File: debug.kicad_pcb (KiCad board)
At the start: 2 copper layers, 56.4 x 42.2 mm, 47 parts, among them J1 ZX62D-AB-5P8, P1 LPC-Link, P2 UART, P3 JTAG, P4 Cortex-Debug, P5 Vout, U1 93C46, U2 PRTR5V0U2X, U3 FT2232H, U4 LD1117S33CTR, X1 12MHz

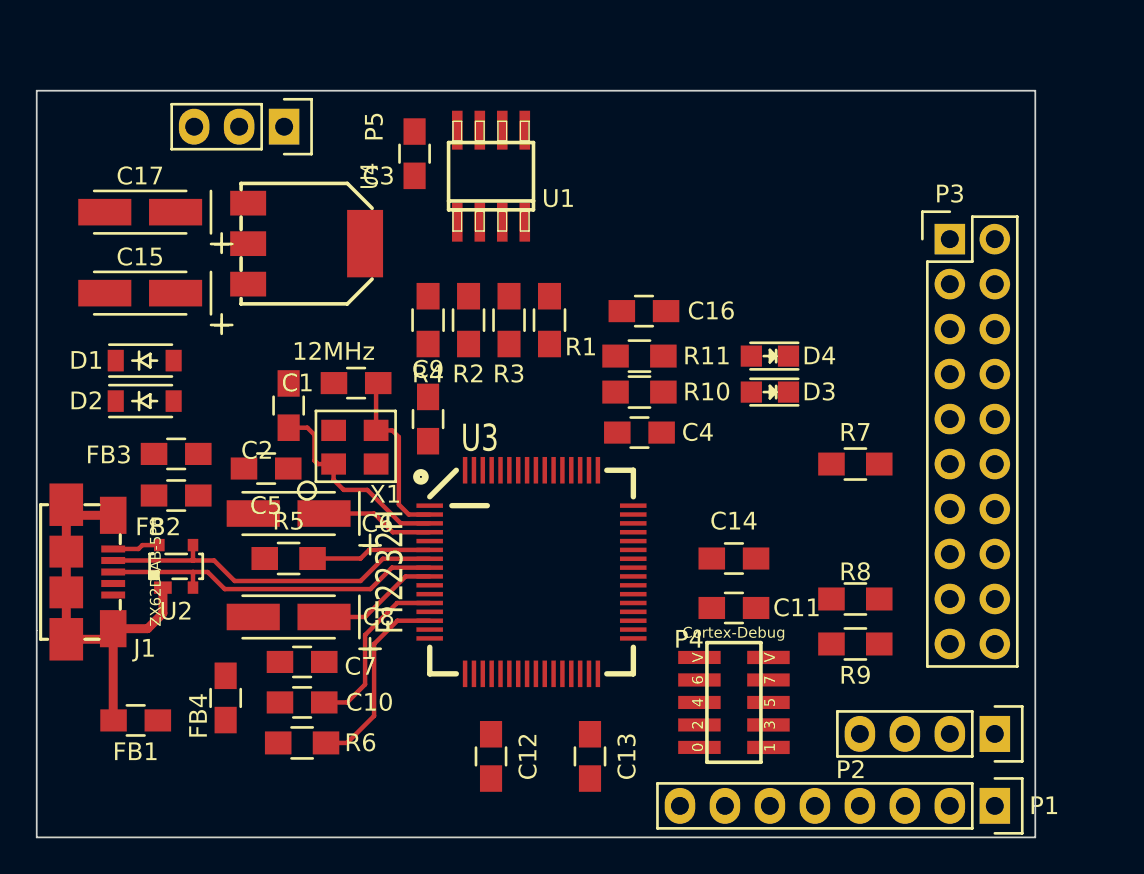
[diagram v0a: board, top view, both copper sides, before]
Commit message: falta plano gnd
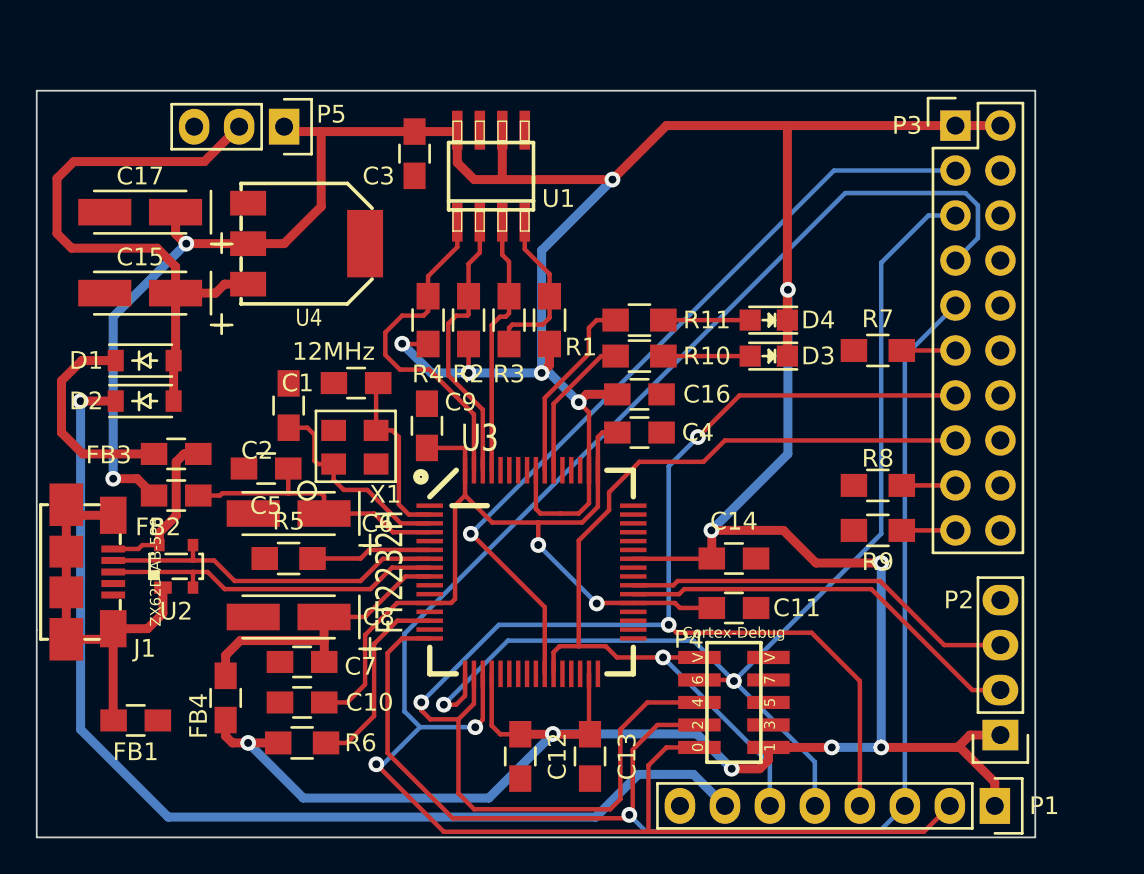
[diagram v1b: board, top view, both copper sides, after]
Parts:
- moved R7 6.54 mm to (124.5, 96.2)
- moved R8 6.54 mm to (124.5, 103.8)
- moved R9 6.54 mm to (124.5, 106.4)
- moved P3 6.42 mm to (128.8, 83.5)
- moved C16 4.71 mm to (111.0, 98.7)
- moved D3 2.03 mm to (118.3, 96.5)
- moved D4 2.03 mm to (118.3, 94.5)
- moved R10 2.03 mm to (111.0, 96.5)
- moved R11 2.03 mm to (111.0, 94.5)
- moved C12 1.65 mm to (104.3, 119.1)
- moved C9 0.39 mm to (99.0, 100.5)
- moved P2 0.32 mm to (131.4, 117.9), turned to 180 degrees
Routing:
- net +3V3: track 0.00 -> 245.5 mm, vias 0 -> 15
- net /FT_TMS: track 0.00 -> 103.5 mm, vias 0 -> 2
- net /FT_TDO: track 0.00 -> 90.4 mm, vias 0 -> 3
- net /FT_TCK: track 0.00 -> 77.7 mm, vias 0 -> 1
- net /FT_TDI: track 0.00 -> 64.8 mm, vias 0 -> 2
- net /5Vin: track 0.00 -> 60.7 mm, vias 0 -> 1
- net /FT_RST: track 0.00 -> 50.9 mm, vias 0 -> 1
- net /FT_TRST: track 0.00 -> 45.5 mm, vias 0 -> 1
- net /USB_JTAG_1.8V: track 9.92 -> 48.6 mm, vias 0 -> 2
- net +5V: track 0.00 -> 34.0 mm
- net /FT_TXD: track 0.00 -> 23.2 mm
- net /FT_RXD: track 0.00 -> 22.3 mm
- net /EECS: track 0.00 -> 19.4 mm
- net /EECLK: track 0.00 -> 15.9 mm
- net /EEDATA: track 0.00 -> 14.8 mm
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
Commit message: pcb terminado, enviado a fabricacion
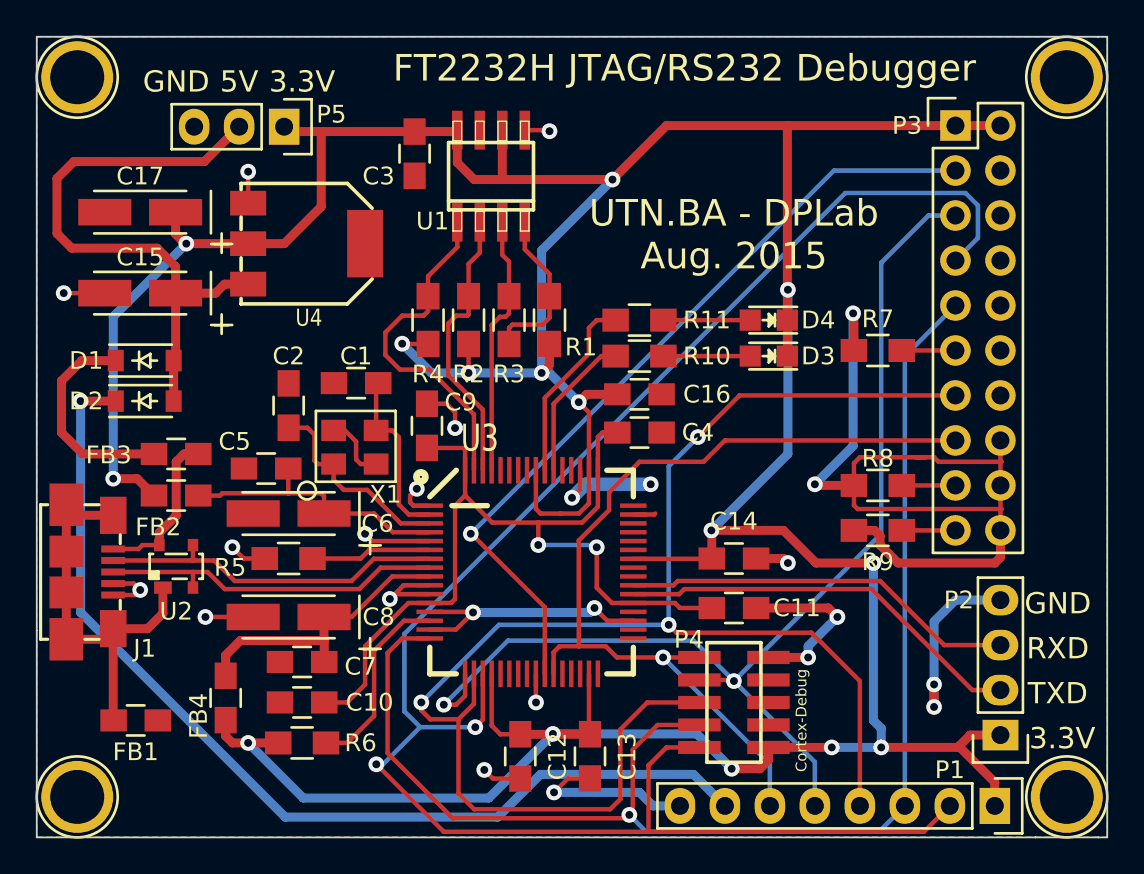
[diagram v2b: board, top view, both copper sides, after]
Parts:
- added P6: MH, Connect:1pin, F.Cu at (79.2, 121.4)
- added P7: MH, Connect:1pin, F.Cu at (135.1, 80.8)
- added P8: MH, Connect:1pin, F.Cu at (79.2, 80.8)
- added P9: MH, Connect:1pin, F.Cu at (135.1, 121.4)
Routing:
- net GND: track 0.00 -> 140.3 mm, vias 0 -> 24
- net /5Vin: track 60.7 -> 56.8 mm
- net /USB_JTAG_1.8V: track 48.6 -> 49.6 mm
- added copper zone on B.Cu, net GND
- added copper zone on F.Cu, net GND
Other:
- board size 56.4 x 42.2 mm -> 60.5 x 45.2 mm
- board text added: "3.3V"
- board text added: "5V"
- board text added: "5Vin"
- board text added: "FT2232H JTAG/RS232 Debugger"
- board text added: "GND"
- board text added: "RST"
- board text added: "RXD"
- board text added: "TCK"
- board text added: "TDI"
- board text added: "TDO"
- board text added: "TMS"
- board text added: "TRST"
- board text added: "TXD"
- board text added: "UTN.BA - DPLab Aug. 2015"
